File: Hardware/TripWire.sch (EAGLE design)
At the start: 50 parts, among them P1 LSP11, P2 LSP11, P3 LSP11, P4 LSP11, P5 LSP11, P6 LSP11, P7 LSP11, X1 GADGETEER-SOCKET

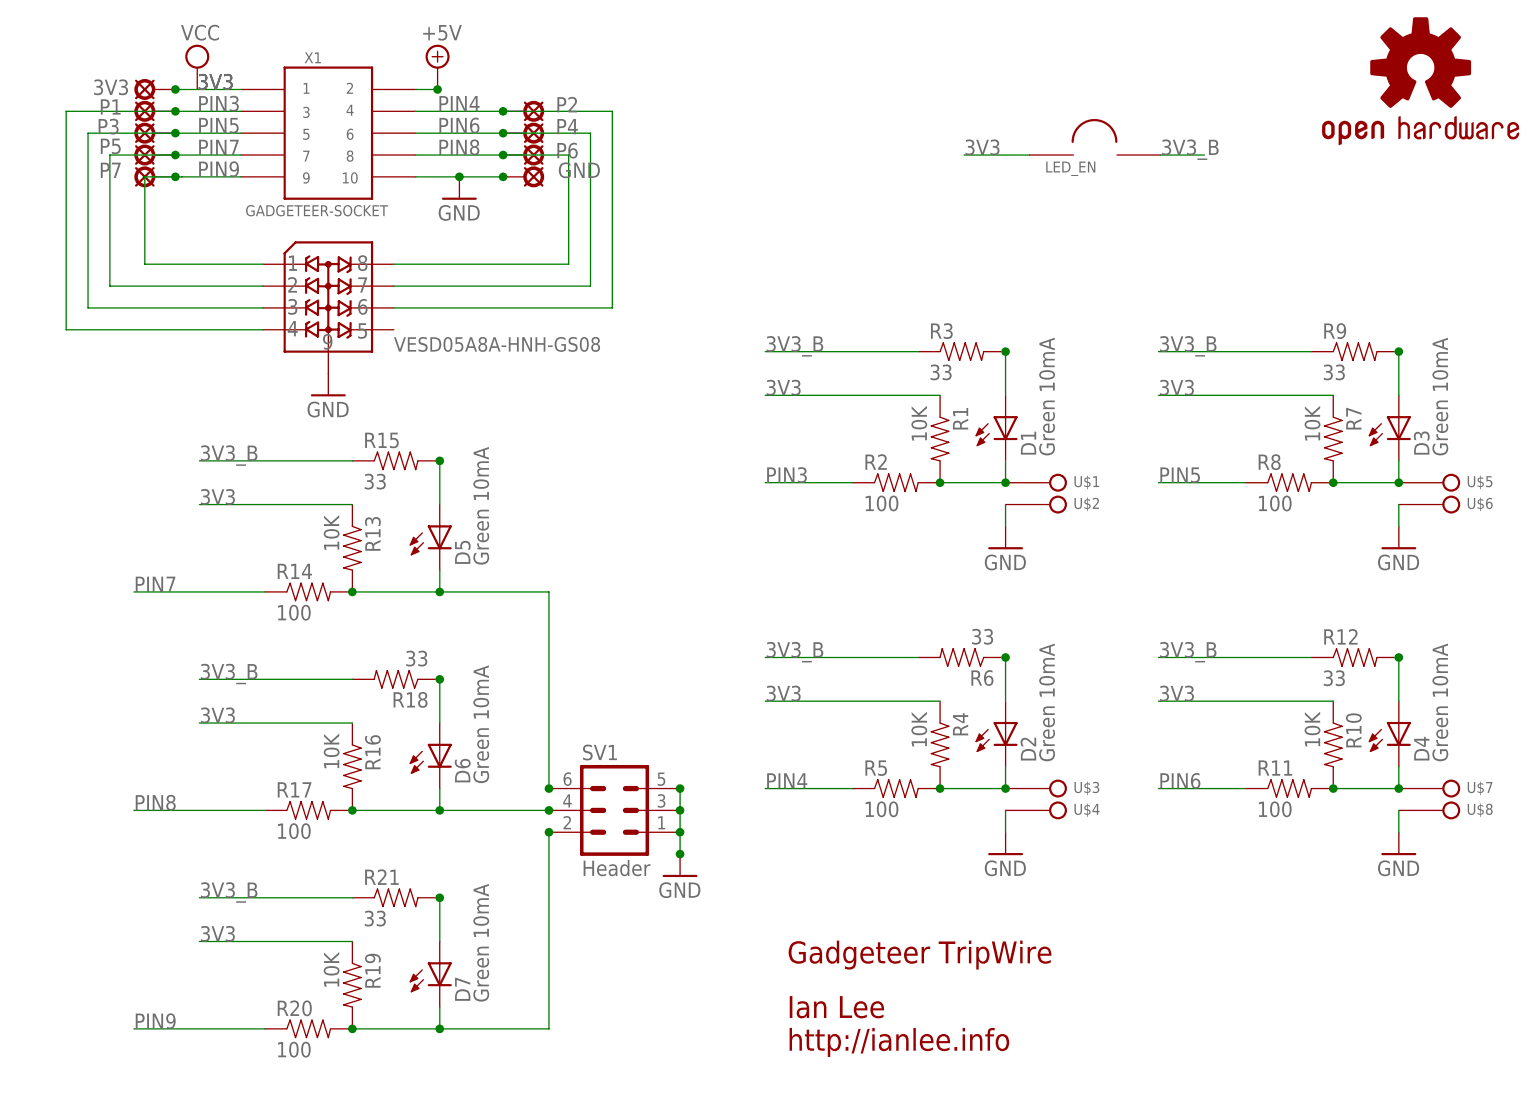
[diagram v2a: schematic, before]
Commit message: Merged 3V3 & 3V3_B nets.
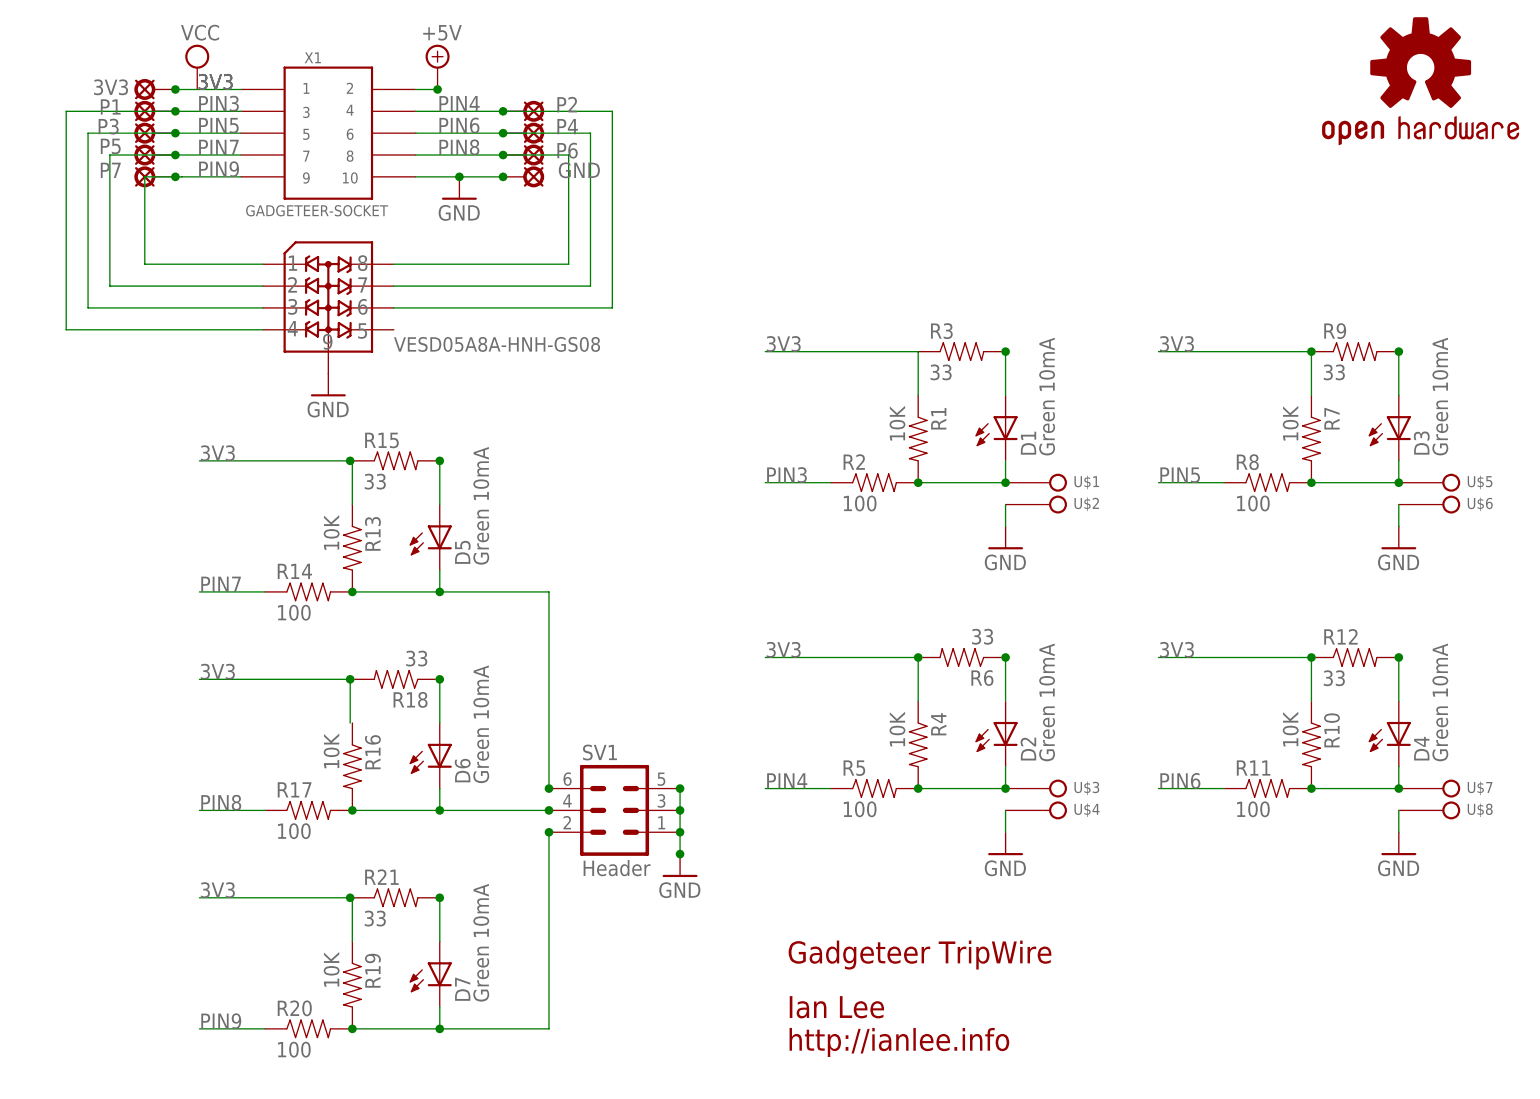
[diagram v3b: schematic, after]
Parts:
- removed LED_EN: SOLDER-JUNCTION, SoftDust:SOLDER-JUNCTION
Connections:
- removed net 3V3_B: LED_EN.P$2, R12.1, R15.1, R18.2, R21.1, R3.1, R6.2, R9.1
- net 3V3: now also R12.1, R15.1, R18.2, R21.1, R3.1, R6.2, R9.1; no longer LED_EN.P$1, R16.1
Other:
- moved on the sheet: R1, R10, R11, R2, R4, R5, R7, R8

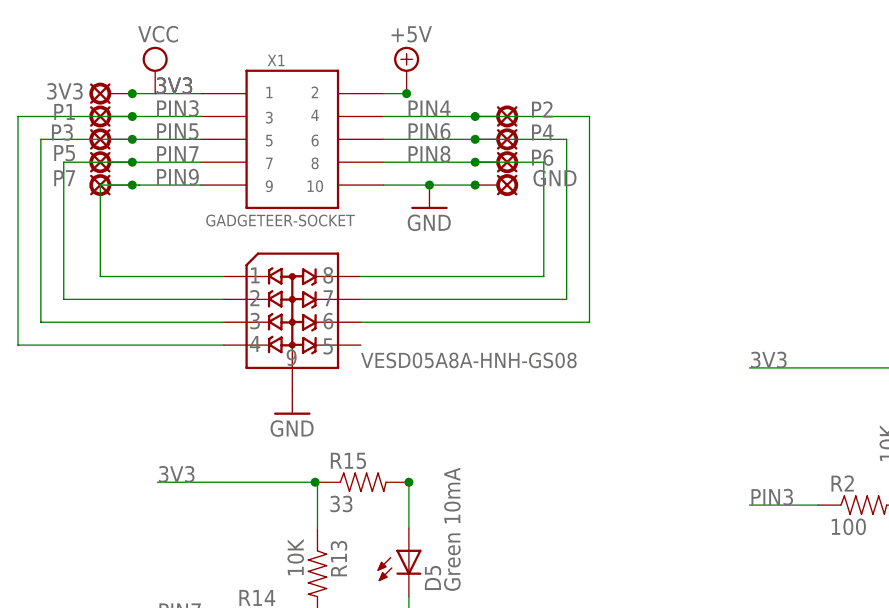
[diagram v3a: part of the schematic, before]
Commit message: Added 100 Ohm resistors to IO pins.
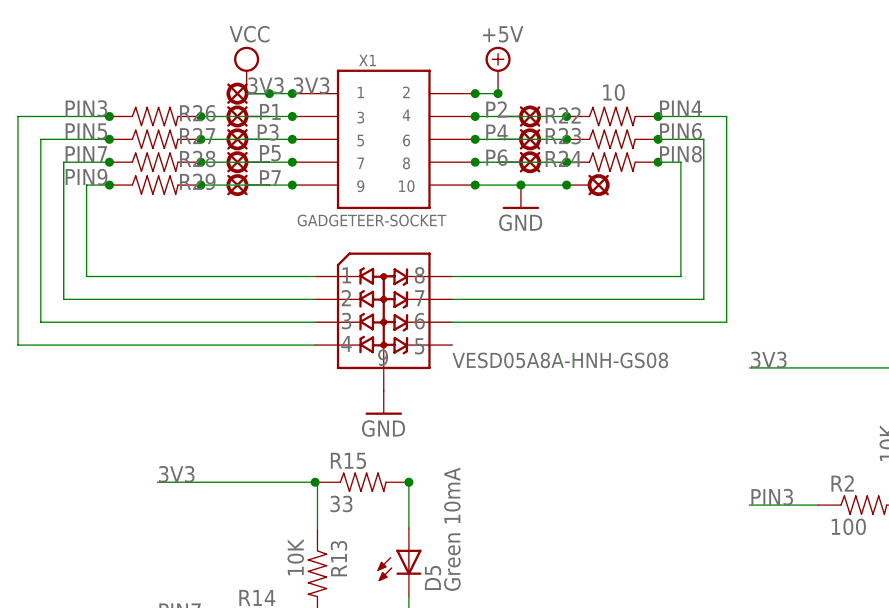
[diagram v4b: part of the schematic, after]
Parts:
- added R22, R23, R24, R26, R27, R28, R29: 10, SparkFun-Resistors:RESISTOR0603-RES
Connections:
- new net N$15: P2.MP, R22.1, X1.P$4
- new net N$16: P4.MP, R23.1, X1.P$6
- new net N$17: P6.MP, R24.1, X1.P$8
- new net N$18: P1.MP, R26.2, X1.P$3
- new net N$19: P3.MP, R27.2, X1.P$5
- new net N$20: P5.MP, R28.2, X1.P$7
- new net N$21: P7.MP, R29.2, X1.P$9
- net PIN3: now also R26.1; no longer P1.MP, X1.P$3
- net PIN4: now also R22.2; no longer P2.MP, X1.P$4
- net PIN5: now also R27.1; no longer P3.MP, X1.P$5
- net PIN6: now also R23.2; no longer P4.MP, X1.P$6
- net PIN7: now also R28.1; no longer P5.MP, X1.P$7
- net PIN8: now also R24.2; no longer P6.MP, X1.P$8
- net PIN9: now also R29.1; no longer P7.MP, X1.P$9
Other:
- moved on the sheet: P1, P2, P3, P4, P5, P6, P7, VESD05A8A-HNH-GS08, X1
